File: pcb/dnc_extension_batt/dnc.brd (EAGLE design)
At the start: 99.8 x 56 mm, 105 parts, among them Q1 IRF9321PBF, Q2 IRF9321PBF, Q3 BSS138, Q5 BSS138, U1 LCD-16X2NOHOLES, U2 74HCT595D

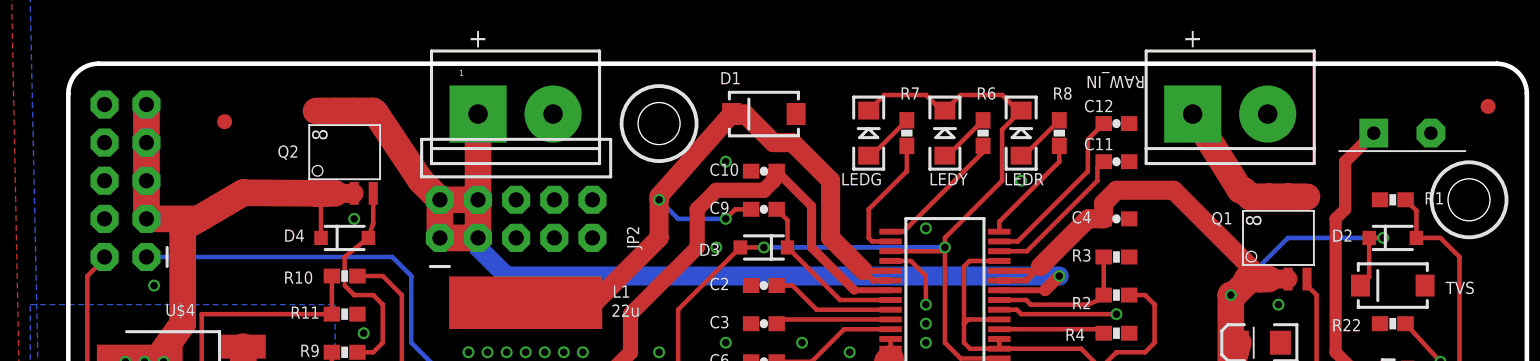
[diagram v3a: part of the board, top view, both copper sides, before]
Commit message: major change correction : - driver led position - add usb for power - correct max 202 voltage problem - titrer connector position - forget line - power trace consideration
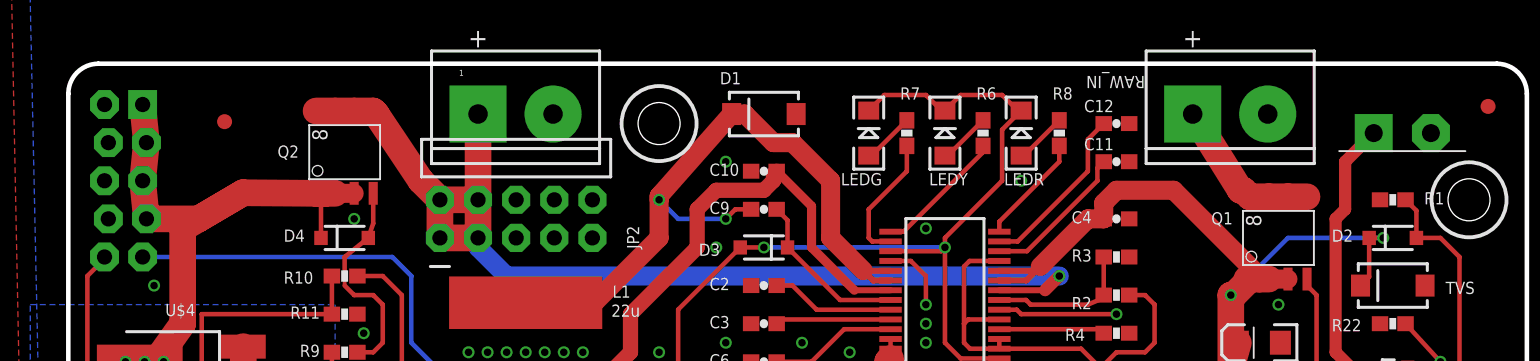
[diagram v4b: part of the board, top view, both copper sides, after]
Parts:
- JP1: device SparkFun:2X5-SHROUDED_LOCK -> pierre_vv:2X5_LOCK
- turned JP1 to 90 degrees
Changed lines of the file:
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@@
 <setting verticaltext="up"/>
 </settings>
-<grid distance="25" unitdist="mil" unit="mm" style="lines" multiple="1" display="yes" altdistance="5" altunitdist="mil" altunit="mil"/>
+<grid distance="25" unitdist="mil" unit="mil" style="lines" multiple="1" display="yes" altdistance="5" altunitdist="mil" altunit="mil"/>
 <layers>
 <layer number="1" name="Top" color="4" fill="1" visible="yes" active="yes"/>
@@
 <element name="JP14" library="SparkFun" package="FIDUCIAL-1X2.5" value="FIDUCIAL1X2.5" x="94.615" y="81.153" smashed="yes" rot="R180"/>
 <element name="JP19" library="SparkFun" package="FIDUCIAL-1X2.5" value="FIDUCIAL1X2.5" x="96.4692" y="2.9642" smashed="yes"/>
-<element name="JP1" library="SparkFun" package="2X5-SHROUDED_LOCK" value="CHARGEUR" x="3.81" y="76.2" smashed="yes" rot="R180">
-<attribute name="VALUE" x="8.636" y="72.009" size="0.8128" layer="27" font="vector" rot="R90"/>
-<attribute name="NAME" x="9.144" y="82.423" size="0.8128" layer="104"/>
-<attribute name="C" value="1" x="3.81" y="76.2" size="1.778" layer="27" rot="R180" display="off"/>
+<element name="JP1" library="pierre_vv" package="2X5_LOCK" value="CHARGEUR" x="3.81" y="76.2" smashed="yes" rot="R90">
+<attribute name="VALUE" x="-0.381" y="71.374" size="0.8128" layer="27" font="vector"/>
+<attribute name="NAME" x="10.033" y="70.866" size="0.8128" layer="104" rot="R270"/>
+<attribute name="C" value="1" x="3.81" y="76.2" size="1.778" layer="27" rot="R90" display="off"/>
 </element>
 <element name="U$2" library="pierre_vv" package="KXKMLOGO" value="LOGO" x="63.5" y="80.01" smashed="yes" rot="MR0"/>
@@
 <attribute name="NAME" x="77.597" y="74.1045" size="0.8128" layer="25" ratio="10" rot="R180"/>
 <attribute name="C" value="1" x="80.645" y="72.39" size="1.778" layer="27" rot="R90" display="off"/>
+<attribute name="OC_FARNELL" value="1831075" x="80.645" y="72.39" size="1.778" layer="27" rot="R90" display="off"/>
 </element>
 <element name="TVS" library="SparkFun" package="SMA-DIODE" value="TVS-30V" x="88.265" y="69.215" smashed="yes" rot="R180">
@@
 <attribute name="NAME" x="15.367" y="78.5495" size="0.8128" layer="25" ratio="10" rot="R180"/>
 <attribute name="C" value="1" x="18.415" y="78.105" size="1.778" layer="27" rot="R90" display="off"/>
+<attribute name="OC_FARNELL" value="1831075" x="18.415" y="78.105" size="1.778" layer="27" rot="R90" display="off"/>
 </element>
 <element name="R9" library="SparkFun-Passives" package="0603-RES" value="100K" x="18.415" y="64.77" smashed="yes" rot="R180">
@@
 <wire x1="90.49" y1="61.915" x2="91.44" y2="62.865" width="0.3048" layer="1"/>
 <wire x1="91.44" y1="62.865" x2="91.44" y2="64.135" width="0.3048" layer="1"/>
-<wire x1="5.207" y1="71.12" x2="5.08" y2="71.12" width="0.3048" layer="16"/>
-<wire x1="5.207" y1="71.12" x2="21.59" y2="71.12" width="0.3048" layer="16"/>
+<wire x1="4.953" y1="71.12" x2="5.08" y2="71.12" width="0.3048" layer="16"/>
+<wire x1="4.953" y1="71.12" x2="21.59" y2="71.12" width="0.3048" layer="16"/>
 <wire x1="21.59" y1="71.12" x2="22.86" y2="69.85" width="0.3048" layer="16"/>
 <wire x1="22.86" y1="69.85" x2="22.86" y2="65.405" width="0.3048" layer="16"/>
@@
 <contactref element="D4" pad="C"/>
 <contactref element="U$4" pad="4"/>
-<wire x1="5.207" y1="81.28" x2="5.207" y2="78.74" width="1.778" layer="1"/>
-<wire x1="5.207" y1="78.74" x2="5.207" y2="76.2" width="1.778" layer="1"/>
-<wire x1="5.207" y1="76.2" x2="5.207" y2="73.66" width="1.778" layer="1"/>
+<wire x1="4.953" y1="81.28" x2="5.207" y2="78.74" width="1.778" layer="1"/>
+<wire x1="5.207" y1="78.74" x2="4.953" y2="76.2" width="1.778" layer="1"/>
+<wire x1="4.953" y1="76.2" x2="5.207" y2="73.66" width="1.778" layer="1"/>
 <wire x1="5.207" y1="73.66" x2="8.6868" y2="73.66" width="1.778" layer="1"/>
 <wire x1="8.6868" y1="73.66" x2="11.6459" y2="75.3999" width="1.778" layer="1"/>

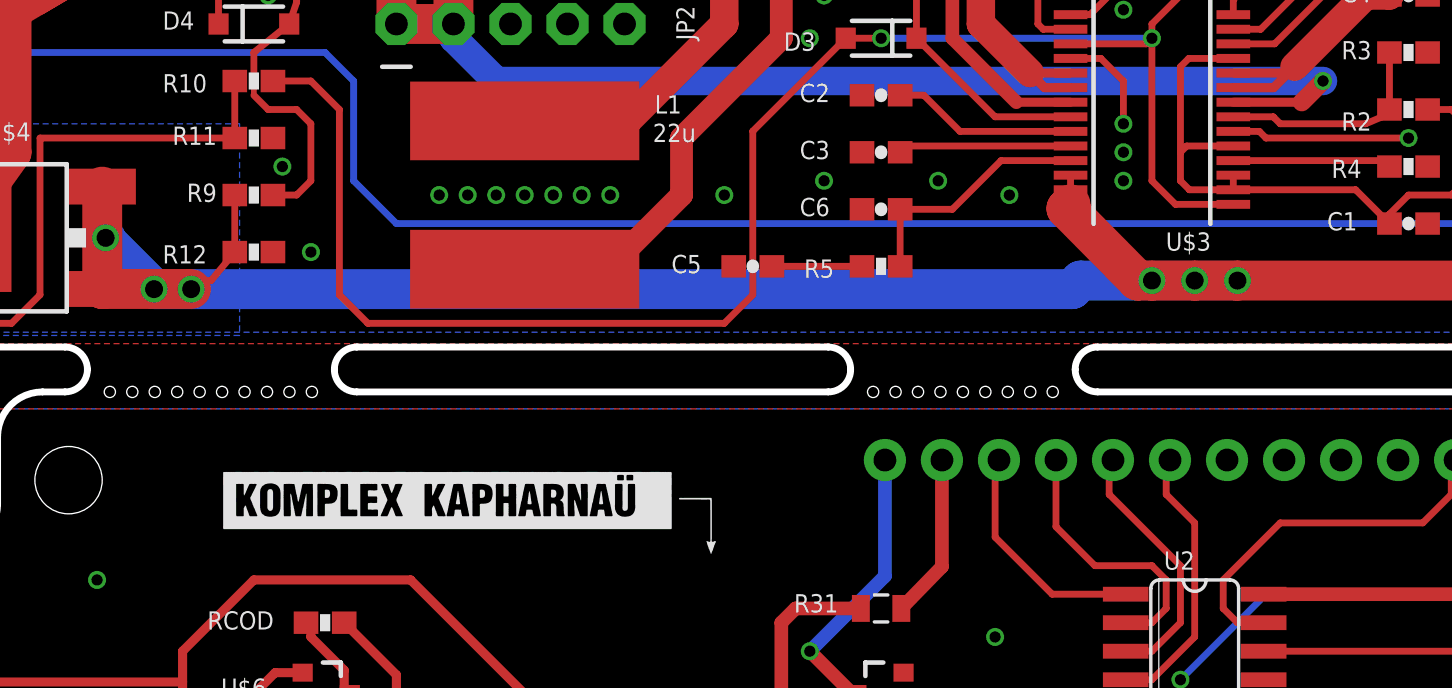
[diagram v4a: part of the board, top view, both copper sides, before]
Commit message: minor change : - logo size - add fuse on led - enclosure
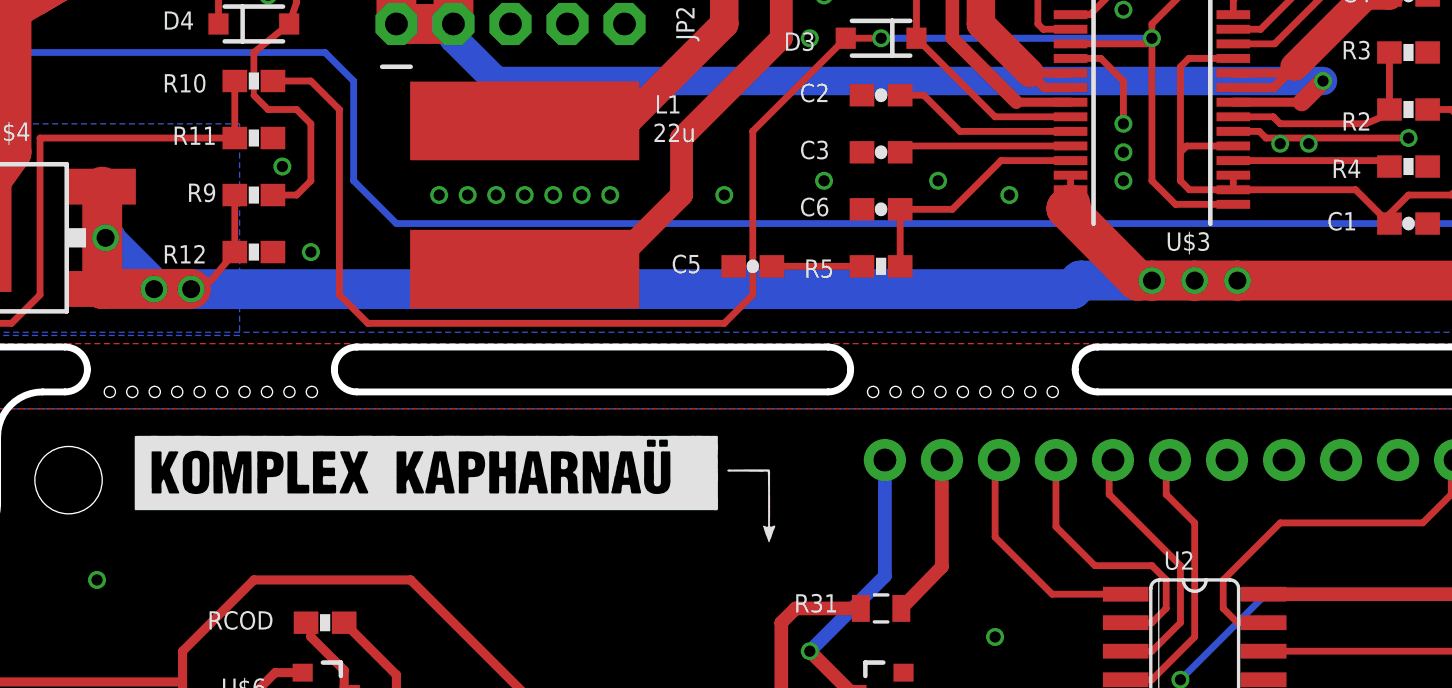
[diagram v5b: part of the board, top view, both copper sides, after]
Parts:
- U$2, U$6MOV: value LOGO -> LOGOSIZE2; device pierre_vv:KXKMLOGO -> pierre_vv:KXKMLOGO2
- moved U$6MOV 12.7 mm to (13.1, 47.1)
- moved U$2 9.16 mm to (71.1, 74.9)
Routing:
- net GND: vias 31 -> 33
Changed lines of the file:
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@@
 <attribute name="C" value="1" x="3.81" y="76.2" size="1.778" layer="27" rot="R90" display="off"/>
 </element>
-<element name="U$2" library="pierre_vv" package="KXKMLOGO" value="LOGO" x="63.5" y="80.01" smashed="yes" rot="MR0"/>
+<element name="U$2" library="pierre_vv" package="KXKMLOGO2" value="LOGOSIZE2" x="71.12" y="74.93" smashed="yes" rot="MR0"/>
 <element name="RAW_IN" library="pierre_vv" package="DNC_IN2_PWR" value="SUPPLY" x="74.93" y="80.645" smashed="yes">
 <attribute name="NAME" x="71.755" y="83.185" size="0.8128" layer="25" rot="SR180"/>
@@
 </element>
 <element name="U$5" library="pierre_vv" package="BOX_SIZE" value="BOITIERBOITIER_FARNELLE_479-0020-0" x="0" y="0" smashed="yes"/>
-<element name="U$6MOV" library="pierre_vv" package="KXKMLOGO" value="LOGO" x="25.175" y="50.88" smashed="yes"/>
+<element name="U$6MOV" library="pierre_vv" package="KXKMLOGO2" value="LOGOSIZE2" x="13.11" y="47.07" smashed="yes"/>
 <element name="U1" library="SparkFun-Displays" package="LCD-16X2_NOHOLES" value="LCD-16X2NOHOLES" x="52.625" y="37.465" rot="MR0"/>
 <element name="C16" library="rcl" package="C0603" value="0.1uF" x="60.325" y="31.115" smashed="yes" rot="R180">
@@
 <via x="80.645" y="17.78" extent="1-16" drill="0.5"/>
 <via x="11.43" y="47.625" extent="1-16" drill="0.5"/>
+<via x="64.135" y="67.056" extent="1-16" drill="0.5"/>
+<via x="65.405" y="67.056" extent="1-16" drill="0.5"/>
 <wire x1="80.775" y1="61.595" x2="84.625" y2="52.965" width="0" layer="19" extent="1-1"/>
 </signal>
